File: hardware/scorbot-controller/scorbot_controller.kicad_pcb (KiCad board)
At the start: 2 copper layers, 185 x 128 mm, 102 parts, among them J1 12V in (CUI PJ-102AH, 2.1 mm), J2 12V in (screw terminal, +/-), J3 E-STOP (NC, in VM line), J4 DD-50 female R/A (robot cable), J5 I2C expansion, J6 Spare TCA9555 I/O, J7 FUSE alt: wire inline 5A fuse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, U1 DROK mini buck, set to 5V, U10 Pololu #4035 DRV8874 (M1), U11 Pololu #4035 DRV8874 (M2), U12 Pololu #4035 DRV8874 (M3), U13 Pololu #4035 DRV8874 (M4), U14 Pololu #4035 DRV8874 (M5), U15 Pololu #4035 DRV8874 (M6), U2 ESP32-DevKitC (WROOM-32D or -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, U5 TCA9555PWR (0x20), U6 ADS1115IDGSR (0x48), U7 ADS1115IDGSR (0x49)

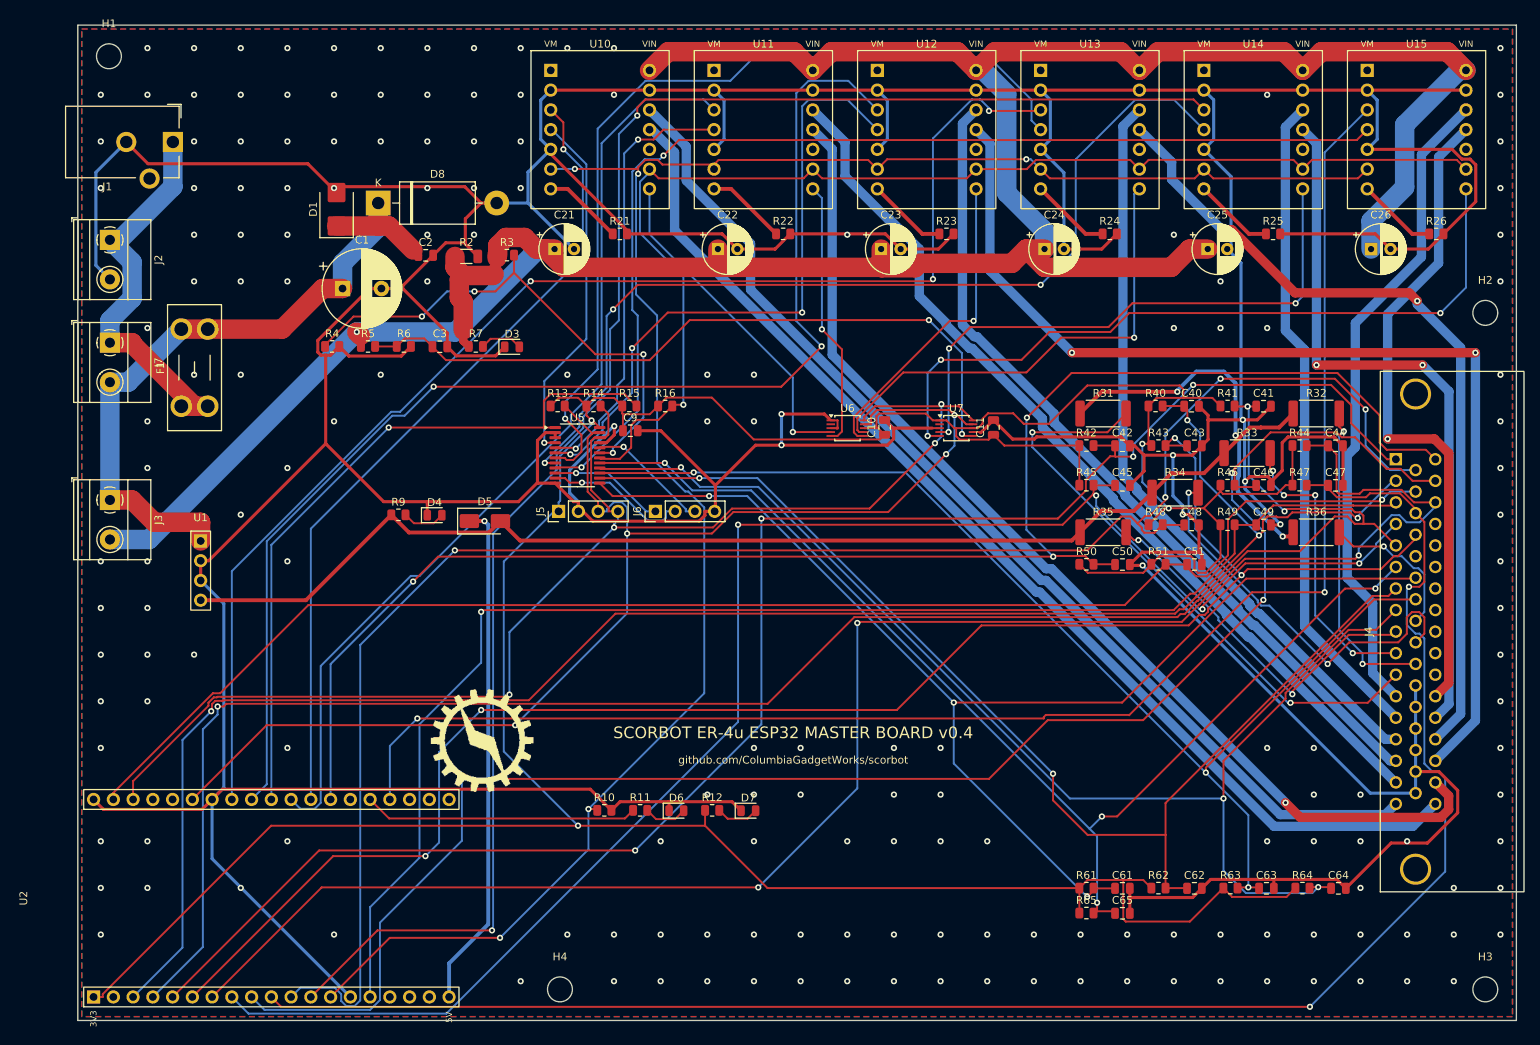
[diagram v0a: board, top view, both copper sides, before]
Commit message: Master board: silkscreen labels and a larger CGW logo
gen_silk.py runs after routing and labels the power inputs (12V IN,
12V IN 2, 18 V max), both fuse options, the E-stop, the TVS choice, the
buck module and its pins, the I2C and GPIO headers pin by pin, the driver
sockets (M1-M6 with joint names), the status LEDs and the DB-50.

It also moves the DevKit's 5V/3V3/GND marks inward, clear of the board
edge and the pins, adds a USB-end arrow, and puts the CGW logo bottom
middle at 23 mm (was 14). Copper, mask and drill gerbers are unchanged;
only F.SilkS differs.
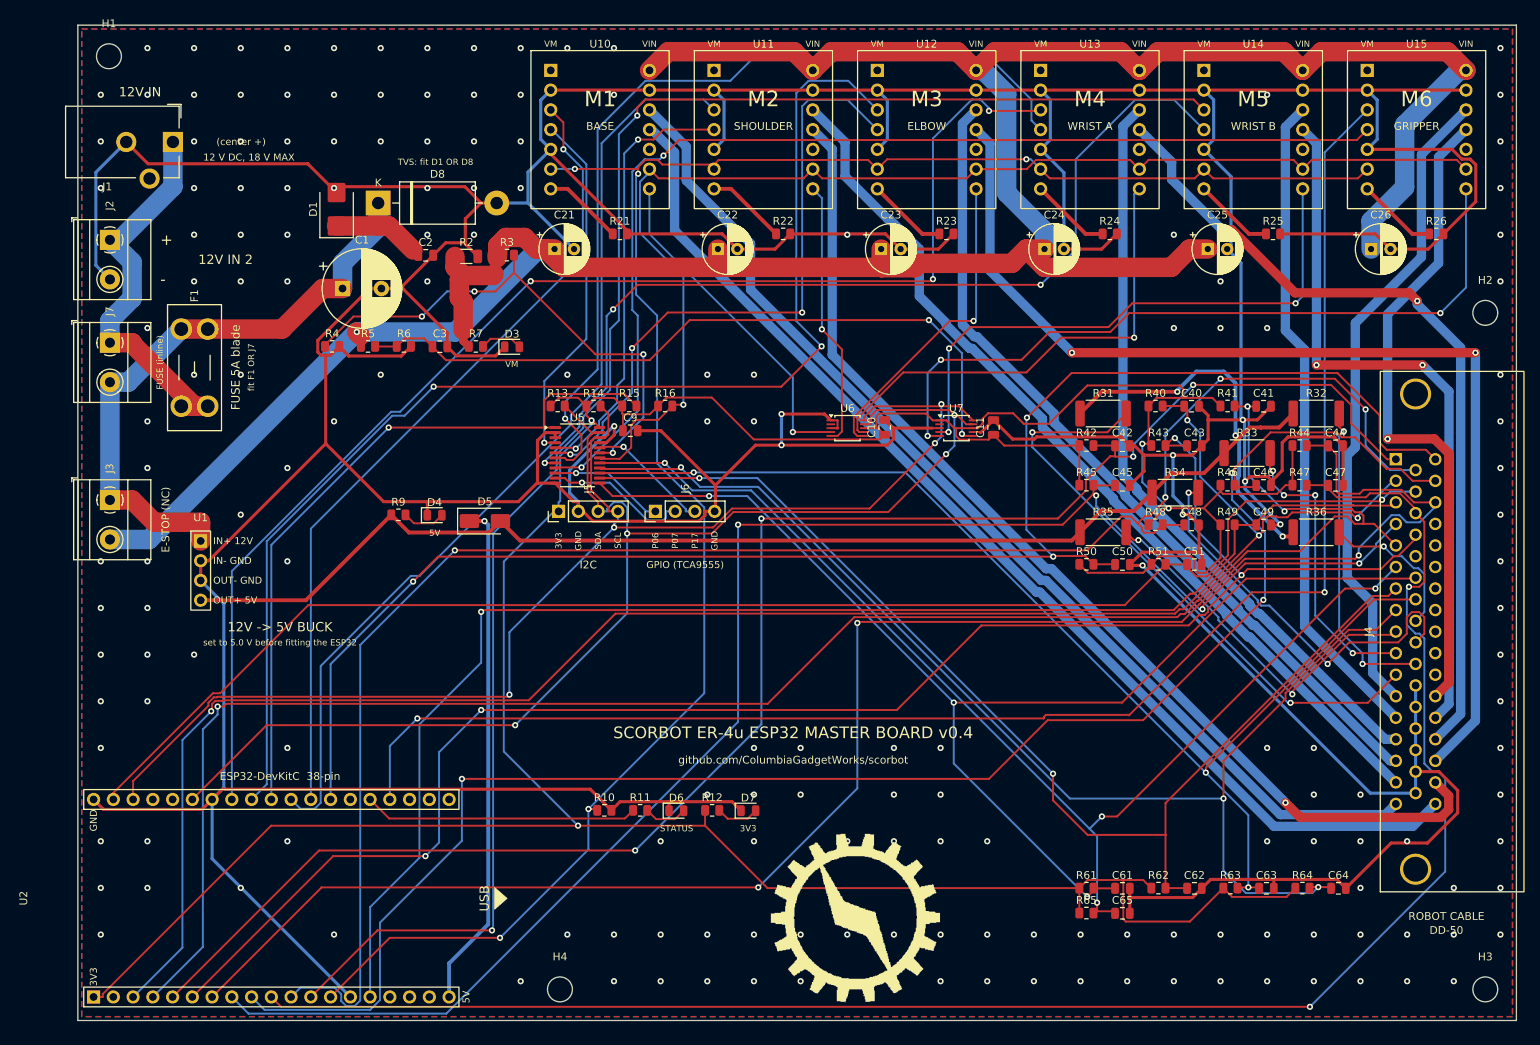
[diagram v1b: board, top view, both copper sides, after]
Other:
- board text added: "(center +)"
- board text added: "+"
- board text added: "-"
- board text added: "12 V DC, 18 V MAX"
- board text added: "12V -> 5V BUCK"
- board text added: "12V IN"
- board text added: "12V IN 2"
- board text added: "3V3"
- board text added: "5V"
- board text added: "BASE"
- board text added: "DD-50"
- board text added: "E-STOP (NC)"
- board text added: "ELBOW"
- board text added: "ESP32-DevKitC 38-pin"
- board text added: "FUSE (inline)"
- board text added: "FUSE 5A blade"
- board text added: "GND"
- board text added: "GPIO (TCA9555)"
- board text added: "GRIPPER"
- board text added: "I2C"
- board text added: "IN+ 12V"
- board text added: "IN- GND"
- board text added: "M1"
- board text added: "M2"
- board text added: "M3"
- board text added: "M4"
- board text added: "M5"
- board text added: "M6"
- board text added: "OUT+ 5V"
- board text added: "OUT- GND"
- board text added: "P06"
- board text added: "P07"
- board text added: "P17"
- board text added: "ROBOT CABLE"
- board text added: "SCL"
- board text added: "SDA"
- board text added: "SHOULDER"
- board text added: "STATUS"
- board text added: "TVS: fit D1 OR D8"
- board text added: "USB"
- board text added: "VM"
- board text added: "WRIST A"
- board text added: "WRIST B"
- board text added: "fit F1 OR J7"
- board text added: "set to 5.0 V before fitting the ESP32"
